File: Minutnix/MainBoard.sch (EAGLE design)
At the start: 32 parts, among them IC1 MEGA8-AI, IC2 74LS47N, IC3 74LS47N

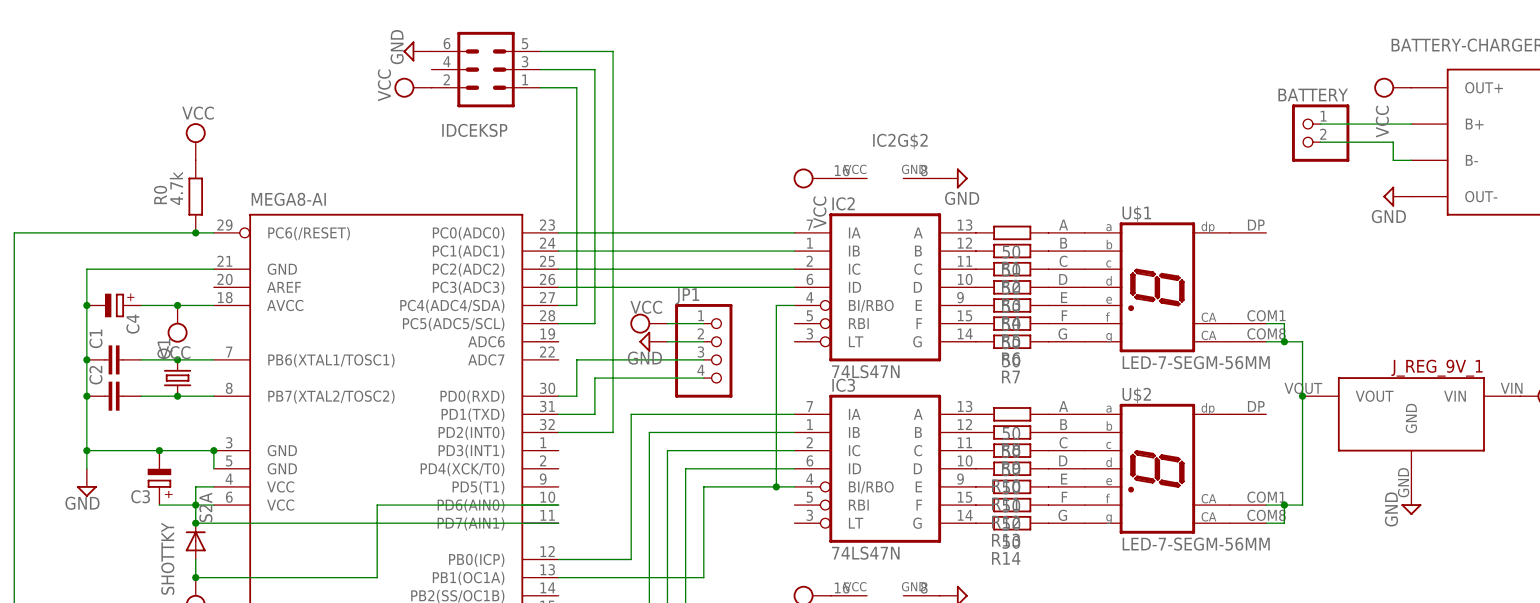
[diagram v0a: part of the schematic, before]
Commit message: First draft of board (correct displays)
Resistors and capacitors not chosen yet,
Goldpin on battery removed - will be directly on board
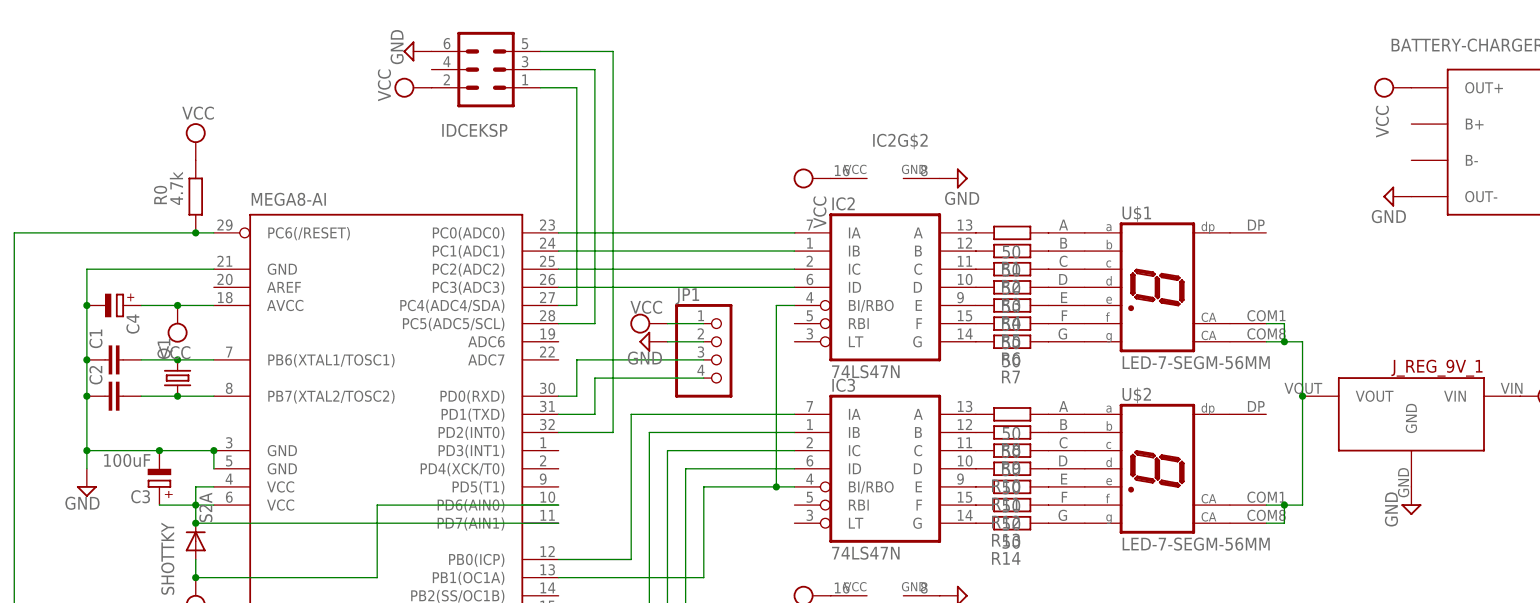
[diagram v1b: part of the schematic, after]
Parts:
- removed BATTERY: (no value), pinhead:PINHD-1X2
- C3: value (none) -> 100uF
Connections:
- removed net N$32: BATTERY.1, U$3.B+
- removed net N$33: BATTERY.2, U$3.B-

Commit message: Wersja 1
Do kubełka 1
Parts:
- removed IC2, IC3: 74LS47N, 74xx-eu:74LS47N
- removed IDCEKSP: (no value), con-harting-ml:ML6
- removed JP1: (no value), pinhead:PINHD-1X4
- removed U$1, U$2: LED-7-SEGM-56MM, BigLED7Segm:LED-7-SEGM-56MM
- added DRIVER1, DRIVER2: 74LS47N, 74xx-eu:74LS47N
- added EKSP: (no value), con-harting-ml:ML6
- added LSDIGIT, MSDIGIT: LED-7-SEGM-56MM, BigLED7Segm:LED-7-SEGM-56MM
- added R15: 50, rcl:R-EU_01005
- added UART: (no value), pinhead:PINHD-1X4
- C1, C2: value (none) -> 22pF
- C3: value 100uF -> 470uF
- C4: value (none) -> 100uF
- Q1: value (none) -> 32.768kHz
- renumbered SHOTTKY to SHOTTKYDIODE
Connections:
- new net N$32: LSDIGIT.DP, R15.1
- new net N$33: IC1.PD5(T1), R15.2
- net GND: now also DRIVER1G$2.GND, DRIVER2G$2.GND, EKSP.6, UART.2; no longer IC2G$2.GND, IC3G$2.GND, IDCEKSP.6, JP1.2
- net N$10: now also DRIVER1G$1.F; no longer IC2G$1.F
- net N$11: now also DRIVER1G$1.G; no longer IC2G$1.G
- net N$12: now also EKSP.1; no longer IDCEKSP.1
- net N$13: now also LSDIGIT.A; no longer U$1.A
- net N$14: now also EKSP.5; no longer IDCEKSP.5
- net N$15: now also LSDIGIT.B; no longer U$1.B
- net N$16: now also LSDIGIT.C; no longer U$1.C
- net N$17: now also LSDIGIT.D; no longer U$1.D
- net N$18: now also LSDIGIT.E; no longer U$1.E
- net N$19: now also LSDIGIT.F; no longer U$1.F
- net N$20: now also EKSP.3; no longer IDCEKSP.3
- net N$21: now also DRIVER2G$1.ID; no longer IC3G$1.ID
- net N$23: now also DRIVER2G$1.IB; no longer IC3G$1.IB
- net N$24: now also DRIVER2G$1.IC; no longer IC3G$1.IC
- net N$25: now also LSDIGIT.G; no longer U$1.G
- net N$26: now also DRIVER1G$1.IA; no longer IC2G$1.IA
- net N$27: now also DRIVER1G$1.IB; no longer IC2G$1.IB
- net N$28: now also DRIVER1G$1.IC; no longer IC2G$1.IC
- net N$29: now also DRIVER1G$1.ID; no longer IC2G$1.ID
- net N$3: now also DRIVER2G$1.IA; no longer IC3G$1.IA
- net N$30: now also UART.4; no longer JP1.4
- net N$31: now also UART.3; no longer JP1.3
- net N$34: now also MSDIGIT.A; no longer U$2.A
- net N$36: now also LSDIGIT.CA1, LSDIGIT.CA8, MSDIGIT.CA1, MSDIGIT.CA8; no longer U$1.CA1, U$1.CA8, U$2.CA1, U$2.CA8
- net N$37: now also MSDIGIT.B; no longer U$2.B
- net N$38: now also MSDIGIT.C; no longer U$2.C
- net N$39: now also MSDIGIT.D; no longer U$2.D
- net N$4: now also DRIVER1G$1.BI/RBO, DRIVER2G$1.BI/RBO; no longer IC2G$1.BI/RBO, IC3G$1.BI/RBO
- net N$40: now also MSDIGIT.E; no longer U$2.E
- net N$41: now also MSDIGIT.F; no longer U$2.F
- net N$42: now also MSDIGIT.G; no longer U$2.G
- net N$44: now also DRIVER2G$1.G; no longer IC3G$1.G
- net N$45: now also DRIVER2G$1.F; no longer IC3G$1.F
- net N$46: now also DRIVER2G$1.E; no longer IC3G$1.E
- net N$47: now also DRIVER2G$1.D; no longer IC3G$1.D
- net N$48: now also DRIVER2G$1.C; no longer IC3G$1.C
- net N$49: now also DRIVER2G$1.B; no longer IC3G$1.B
- net N$5: now also DRIVER1G$1.A; no longer IC2G$1.A
- net N$50: now also DRIVER2G$1.A; no longer IC3G$1.A
- net N$6: now also DRIVER1G$1.B; no longer IC2G$1.B
- net N$7: now also DRIVER1G$1.C; no longer IC2G$1.C
- net N$8: now also DRIVER1G$1.D; no longer IC2G$1.D
- net N$9: now also DRIVER1G$1.E; no longer IC2G$1.E
- net VCC: now also DRIVER1G$2.VCC, DRIVER2G$2.VCC, EKSP.2, UART.1; no longer IC2G$2.VCC, IC3G$2.VCC, IDCEKSP.2, JP1.1
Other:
- moved on the sheet: J_REG_9V_1, R1, R10, R11, R12, R13, R14, R2, R3, R4, R5, R6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

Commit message: Archivisation and actualisation
Archivisation of 1 version of boards
New version of boards
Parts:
- removed DRIVER1, DRIVER2: 74LS47N, 74xx-eu:74LS47N
- removed EKSP: (no value), con-harting-ml:ML6
- added C10, C5, C6, C7, C8: 0.1uF, rcl:CPOL-EU140CLH-1010
- added C9: (no value), rcl:CPOL-EU140CLH-1010
- added GND, PAD1, PAD10, PAD11, PAD12, PAD13, PAD14, PAD2, PAD3, PAD4, PAD5, PAD6, PAD7, PAD8, PAD9, VCC: WIREPADSMD5-2,5, wirepad:WIREPADSMD5-2,5
- added IC2, IC3, IC4, IC5: TPIC6C596PW, tpic:TPIC6C596PW
- added LSDIGIT1, MSDIGIT1: LED-7-SEGM-56MM, BigLED7Segm:LED-7-SEGM-56MM
- added PHOTORES: A1050_09, photo-elements:A1050_09
- added Q2: (no value), semicon-smd-ipc:NPN-TRANSISTOR_SOT23
- added R16, R17, R18, R19, R20, R21, R22, R23, R24, R25, R26, R27, R28: 50, rcl:R-EU_01005
- added R29: 10k, rcl:R-EU_01005
- added R30, R33: 4.7k, rcl:R-EU_01005
- added R31: 47k, rcl:R-EU_01005
- added R32: 7.05k, rcl:R-EU_01005
- added SG1: F/CM12P, buzzer:F/CM12P
- added U$1: PCF8574AT, i2c:PCF8574AT
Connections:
- new net N$43: IC2G$1.Q7, R8.2
- new net N$51: MSDIGIT1.A, R22.1
- new net N$52: MSDIGIT1.B, R23.1
- new net N$53: MSDIGIT1.C, R24.1
- new net N$54: MSDIGIT1.D, R25.1
- new net N$55: MSDIGIT1.E, R26.1
- new net N$56: MSDIGIT1.F, R27.1
- new net N$57: MSDIGIT1.G, R28.1
- new net N$58: IC3G$1.Q0, R9.2
- new net N$59: IC3G$1.Q1, R10.2
- new net N$60: IC3G$1.Q2, R11.2
- new net N$61: IC3G$1.Q3, R12.2
- new net N$62: IC3G$1.Q4, R13.2
- new net N$63: IC3G$1.Q5, R14.2
- new net N$64: IC3G$1.Q6, R15.2
- new net N$65: IC3G$1.Q7, R16.2
- new net N$66: IC4G$1.Q0, R17.2
- new net N$67: IC4G$1.Q1, R18.2
- new net N$68: IC4G$1.Q2, R19.2
- new net N$69: IC4G$1.Q3, R20.2
- new net N$70: IC4G$1.Q4, R21.2
- new net N$71: IC4G$1.Q5, R22.2
- new net N$72: IC4G$1.Q6, R23.2
- new net N$73: IC4G$1.Q7, R24.2
- new net N$74: IC5G$1.Q0, R25.2
- new net N$75: IC5G$1.Q1, R26.2
- new net N$76: IC5G$1.Q2, R27.2
- new net N$77: IC5G$1.Q3, R28.2
- new net N$78: IC3G$1.DO, IC4G$1.DI
- new net N$79: IC4G$1.DO, IC5G$1.DI
- new net N$80: IC2G$1.DO, IC3G$1.DI
- new net N$81: IC1.PC5(ADC5/SCL), U$1IC$1.SCL
- new net N$82: IC1.PC3(ADC3), PAD11.P
- new net N$83: IC1.PB0(ICP), PAD9.P
- new net N$84: IC1.PD5(T1), PAD10.P
- new net N$85: PAD1.P, U$1IC$1.P0
- new net N$86: PAD2.P, U$1IC$1.P1
- new net N$87: PAD3.P, U$1IC$1.P2
- new net N$88: PAD4.P, U$1IC$1.P3
- new net N$89: PAD5.P, U$1IC$1.P4
- new net N$90: PAD6.P, U$1IC$1.P5
- new net N$91: PAD7.P, U$1IC$1.P6
- new net N$92: PAD8.P, U$1IC$1.P7
- new net N$93: IC1.ADC6, PHOTORES.2, R31.1
- net GND: now also C10.-, C5.-, C6.-, C7.-, C8.-, C9.-, GND.P, IC2P.GND, IC3P.GND, IC4P.GND, IC5P.GND, PHOTORES.1, Q2.E, R32.2, U$1IC$1.A0, U$1IC$1.A1, U$1IC$1.A2, U$1PWR.GND; no longer DRIVER1G$2.GND, DRIVER2G$2.GND, EKSP.6
- net N$10: now also IC2G$1.Q5; no longer DRIVER1G$1.F
- net N$11: now also IC2G$1.Q6; no longer DRIVER1G$1.G
- net N$12: now also IC1.PC0(ADC0), PAD14.P; no longer EKSP.1, IC1.PC4(ADC4/SDA)
- net N$14: now also IC1.PC1(ADC1), PAD13.P; no longer EKSP.5, IC1.PD2(INT0)
- net N$20: now also IC1.PC2(ADC2), PAD12.P; no longer EKSP.3, IC1.PC5(ADC5/SCL)
- net N$21: now also Q2.B, R30.1; no longer DRIVER2G$1.ID, IC1.PB5(SCK), USBASP.3
- net N$23: now also IC2G$1.DI; no longer DRIVER2G$1.IB, USBASP.4
- net N$24: now also IC2G$1.SCLR, IC3G$1.SCLR, IC4G$1.SCLR, IC5G$1.SCLR, R29.1; no longer DRIVER2G$1.IC, IC1.PB4(MISO), USBASP.1
- net N$26: now also IC1.PB5(SCK), IC2G$1.SCK, IC3G$1.SCK, IC4G$1.SCK, IC5G$1.SCK, USBASP.3; no longer DRIVER1G$1.IA, IC1.PC0(ADC0)
- net N$27: now also IC1.PB4(MISO), IC2G$1.RCK, IC3G$1.RCK, IC4G$1.RCK, IC5G$1.RCK, USBASP.1; no longer DRIVER1G$1.IB, IC1.PC1(ADC1)
- net N$28: now also J_REG_9V_1.VOUT, LSDIGIT.CA1, LSDIGIT.CA8, LSDIGIT1.CA1, LSDIGIT1.CA8, MSDIGIT.CA1, MSDIGIT.CA8, MSDIGIT1.CA1, MSDIGIT1.CA8, R31.2; no longer DRIVER1G$1.IC, IC1.PC2(ADC2)
- net N$29: now also Q2.C, SG1.2; no longer DRIVER1G$1.ID, IC1.PC3(ADC3)
- net N$3: now also IC1.PB1(OC1A), R30.2; no longer DRIVER2G$1.IA, IC1.PB0(ICP)
- net N$32: now also C10.+, IC1.AREF, R32.1, R33.2; no longer LSDIGIT.DP, R15.1
- net N$33: now also IC1.PC4(ADC4/SDA), U$1IC$1.SDA; no longer IC1.PD5(T1), R15.2
- net N$36: now also IC1.PD2(INT0), U$1IC$1./INT; no longer J_REG_9V_1.VOUT, LSDIGIT.CA1, LSDIGIT.CA8, MSDIGIT.CA1, MSDIGIT.CA8
- net N$4: now also IC1.PB2(SS/OC1B), IC2G$1.G, IC3G$1.G, IC4G$1.G, IC5G$1.G; no longer DRIVER1G$1.BI/RBO, DRIVER2G$1.BI/RBO, IC1.PB1(OC1A)
- net N$44: now also LSDIGIT1.A, R15.1; no longer DRIVER2G$1.G, R14.2
- net N$45: now also LSDIGIT1.B, R16.1; no longer DRIVER2G$1.F, R13.2
- net N$46: now also LSDIGIT1.C, R17.1; no longer DRIVER2G$1.E, R12.2
- net N$47: now also LSDIGIT1.D, R18.1; no longer DRIVER2G$1.D, R11.2
- net N$48: now also LSDIGIT1.E, R19.1; no longer DRIVER2G$1.C, R10.2
- net N$49: now also LSDIGIT1.F, R20.1; no longer DRIVER2G$1.B, R9.2
- net N$5: now also IC2G$1.Q0; no longer DRIVER1G$1.A
- net N$50: now also LSDIGIT1.G, R21.1; no longer DRIVER2G$1.A, R8.2
- net N$6: now also IC2G$1.Q1; no longer DRIVER1G$1.B
- net N$7: now also IC2G$1.Q2; no longer DRIVER1G$1.C
- net N$8: now also IC2G$1.Q3; no longer DRIVER1G$1.D
- net N$9: now also IC2G$1.Q4; no longer DRIVER1G$1.E
- net VCC: now also C5.+, C6.+, C7.+, C8.+, C9.+, IC2P.VCC, IC3P.VCC, IC4P.VCC, IC5P.VCC, R29.2, R33.1, SG1.1, U$1PWR.VCC, VCC.P; no longer DRIVER1G$2.VCC, DRIVER2G$2.VCC, EKSP.2
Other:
- moved on the sheet: J_REG_9V_1, LSDIGIT, MSDIGIT, R1, R10, R11, R12, R13, R14, R15, R2, R3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

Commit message: Minor board changes
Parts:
- added LED1, LED2: (no value), led:LED5MM
- added R34, R35: 50, rcl:R-EU_R1206
- R0, R1, R10, R11, R12, R13, R14, R15, R16, R17, R18, R19, R2, R20, R21, R22, R23, R24, R25, R26, R27, R28, R29, R3, R30, R31, R32, R33, R4, R5, R6, R7, R8, R9: device rcl:R-EU_01005 -> rcl:R-EU_R1206
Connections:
- new net N$94: LED1.C, R34.1
- new net N$95: LED2.C, R35.1
- new net N$96: IC3G$1.Q6, R34.2
- new net N$97: IC3G$1.Q7, R35.2
- net N$64: now also IC4G$1.Q0; no longer IC3G$1.Q6
- net N$65: now also IC4G$1.Q1; no longer IC3G$1.Q7
- net N$66: now also IC4G$1.Q2; no longer IC4G$1.Q0
- net N$67: now also IC4G$1.Q3; no longer IC4G$1.Q1
- net N$68: now also IC4G$1.Q4; no longer IC4G$1.Q2
- net N$69: now also IC4G$1.Q5; no longer IC4G$1.Q3
- net N$70: now also IC4G$1.Q6; no longer IC4G$1.Q4
- net N$71: now also IC4G$1.Q7; no longer IC4G$1.Q5
- net N$72: now also IC5G$1.Q0; no longer IC4G$1.Q6
- net N$73: now also IC5G$1.Q1; no longer IC4G$1.Q7
- net N$74: now also IC5G$1.Q2; no longer IC5G$1.Q0
- net N$75: now also IC5G$1.Q3; no longer IC5G$1.Q1
- net N$76: now also IC5G$1.Q4; no longer IC5G$1.Q2
- net N$77: now also IC5G$1.Q5; no longer IC5G$1.Q3
- net VCC: now also LED1.A, LED2.A
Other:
- moved on the sheet: LSDIGIT1, MSDIGIT1, R15, R16, R17, R18, R19, R20, R21, R22, R23, R24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

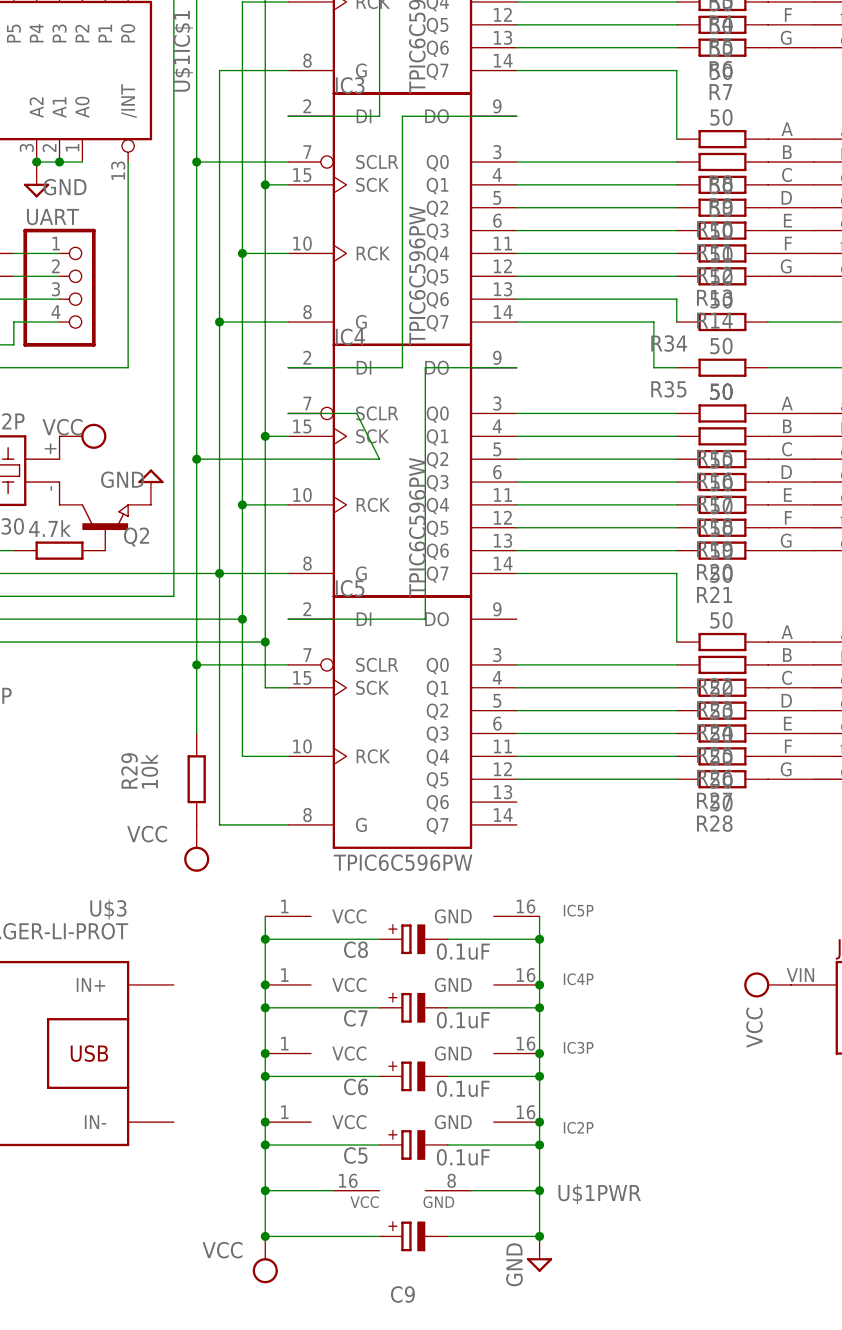
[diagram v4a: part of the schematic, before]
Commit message: Pullup for displays
+removed trash
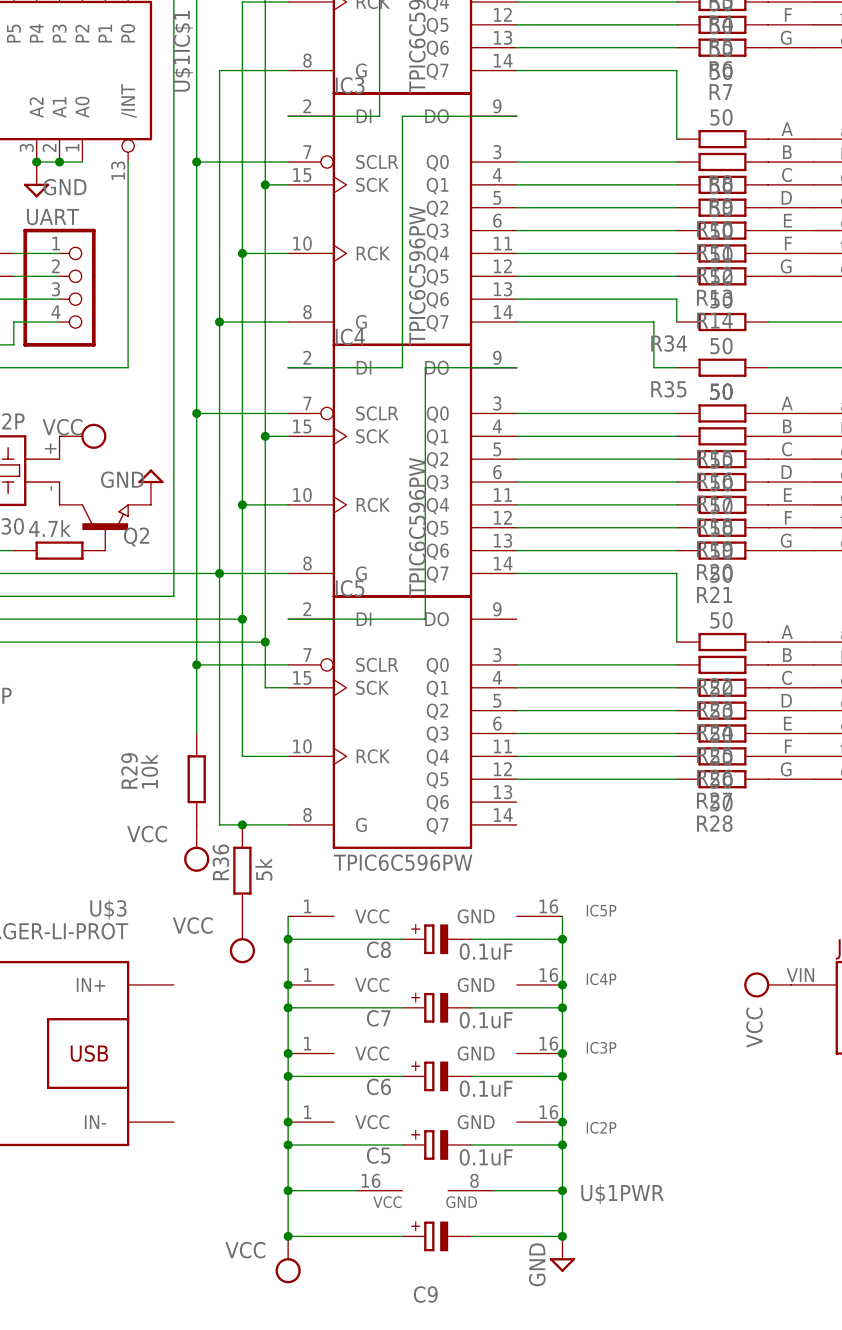
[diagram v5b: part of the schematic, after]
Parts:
- added R36: 5k, rcl:R-EU_R1206
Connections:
- net N$4: now also R36.1
- net VCC: now also R36.2
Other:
- moved on the sheet: C5, C6, C7, C8, C9, IC2P, IC3P, IC4P, IC5P, U$1PWR
